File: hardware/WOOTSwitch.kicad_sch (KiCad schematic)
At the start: 67 parts, among them J1 Mini-DIN-4-G, J10 POWSEL, J11 TWI, J12 TWI, J2 Mini-DIN-4-G, J7 Barrel_Jack_MountingPin, J8 EXT_POW, J9 SW1, Q1 MMBT3904, Q11 2N7002, Q15 2N7002, Q2 MMBT3904, Q3 MMBT3904, Q4 MMBT3904, Q5 MMBT3904, Q6 MMBT3904, Q8 MMBT3904, Q9 2N7002, SW1 Switch1, U1 Pico, U2 LM1117-5.0

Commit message: Rebrand as WOOTSwitch
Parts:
- removed C1: 100uF, Capacitor_THT:CP_Radial_D6.3mm_P2.50mm, symbol Device:C_Polarized_US
- removed SW1: Switch1, Button_Switch_THT:SW_SPST_Omron_B3F-315x_Angled, symbol Switch:SW_Push
- added C1, C15: 47uF, Capacitor_SMD:C_1206_3216Metric, symbol Device:C
- added SW2: 1825910-6, hootswitch:SW_1825910-6-4, symbol hootswitch:1825910-6
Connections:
- net GND: now also C1.2, C15.2, SW2.4
- net SWITCH: now also SW2.2
- net at D7.2 (A), J10.1 (Pin_1), U2.2 (VO): now also C1.1, C15.1
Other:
- sheet hootswitch-computers renamed WOOTSwitch-computers
- sheet WOOTSwitch-computers: file hootswitch-computers.kicad_sch -> WOOTSwitch-computers.kicad_sch
- company: (none) -> Joe's Computer Museum
- title: hootswitch -> WOOTSwitch
- moved on the sheet: D7, J10

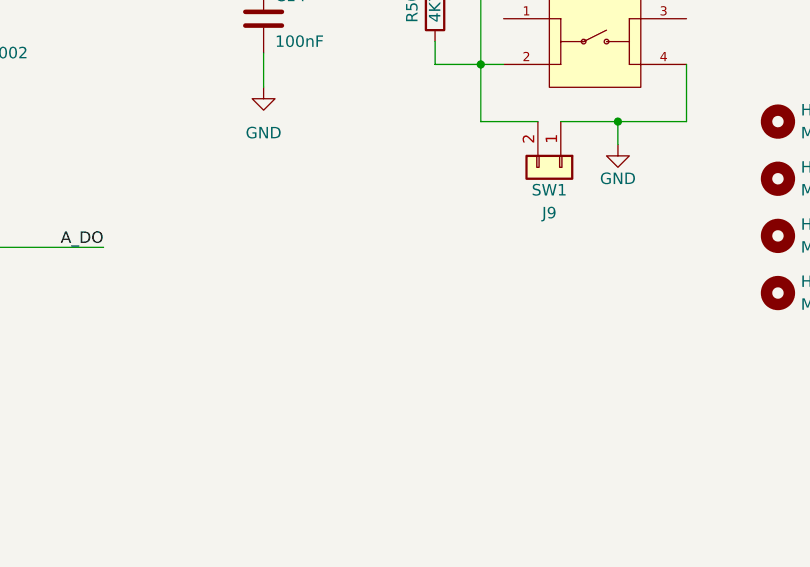
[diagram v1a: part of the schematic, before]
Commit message: Add sheet for power net
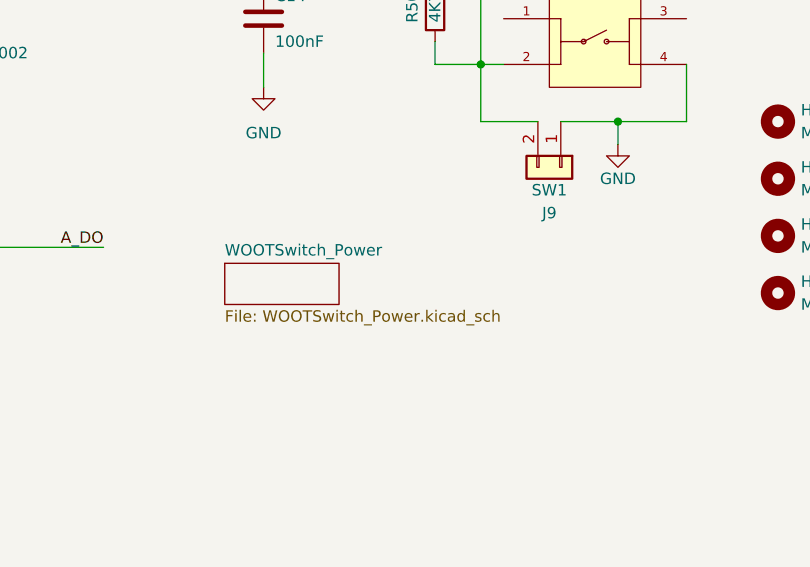
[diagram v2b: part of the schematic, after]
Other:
- added sheet WOOTSwitch_Power (WOOTSwitch_Power.kicad_sch)
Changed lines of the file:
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@@
+		)
+	)
+	(sheet
+		(at 129.032 225.298)
+		(size 12.7 4.572)
+		(exclude_from_sim no)
+		(in_bom yes)
+		(on_board yes)
+		(dnp no)
+		(fields_autoplaced yes)
+		(stroke
+			(width 0.1524)
+			(type solid)
+		)
+		(fill
+			(color 0 0 0 0.0000)
+		)
+		(property "Sheetname" "WOOTSwitch_Power"
+			(at 129.032 224.5864 0)
+			(effects
+				(font
+					(size 1.27 1.27)
+				)
+				(justify left bottom)
+			)
+		)
+		(property "Sheetfile" "WOOTSwitch_Power.kicad_sch"
+			(at 129.032 230.4546 0)
+			(effects
+				(font
+					(size 1.27 1.27)
+				)
+				(justify left top)
+			)
+		)
+		(instances
+			(project "WOOTSwitch"
+				(path "/b47c0368-c762-4e4f-89b1-8c49875ea556"
+					(page "3")
+				)
+			)
 		)
 	)

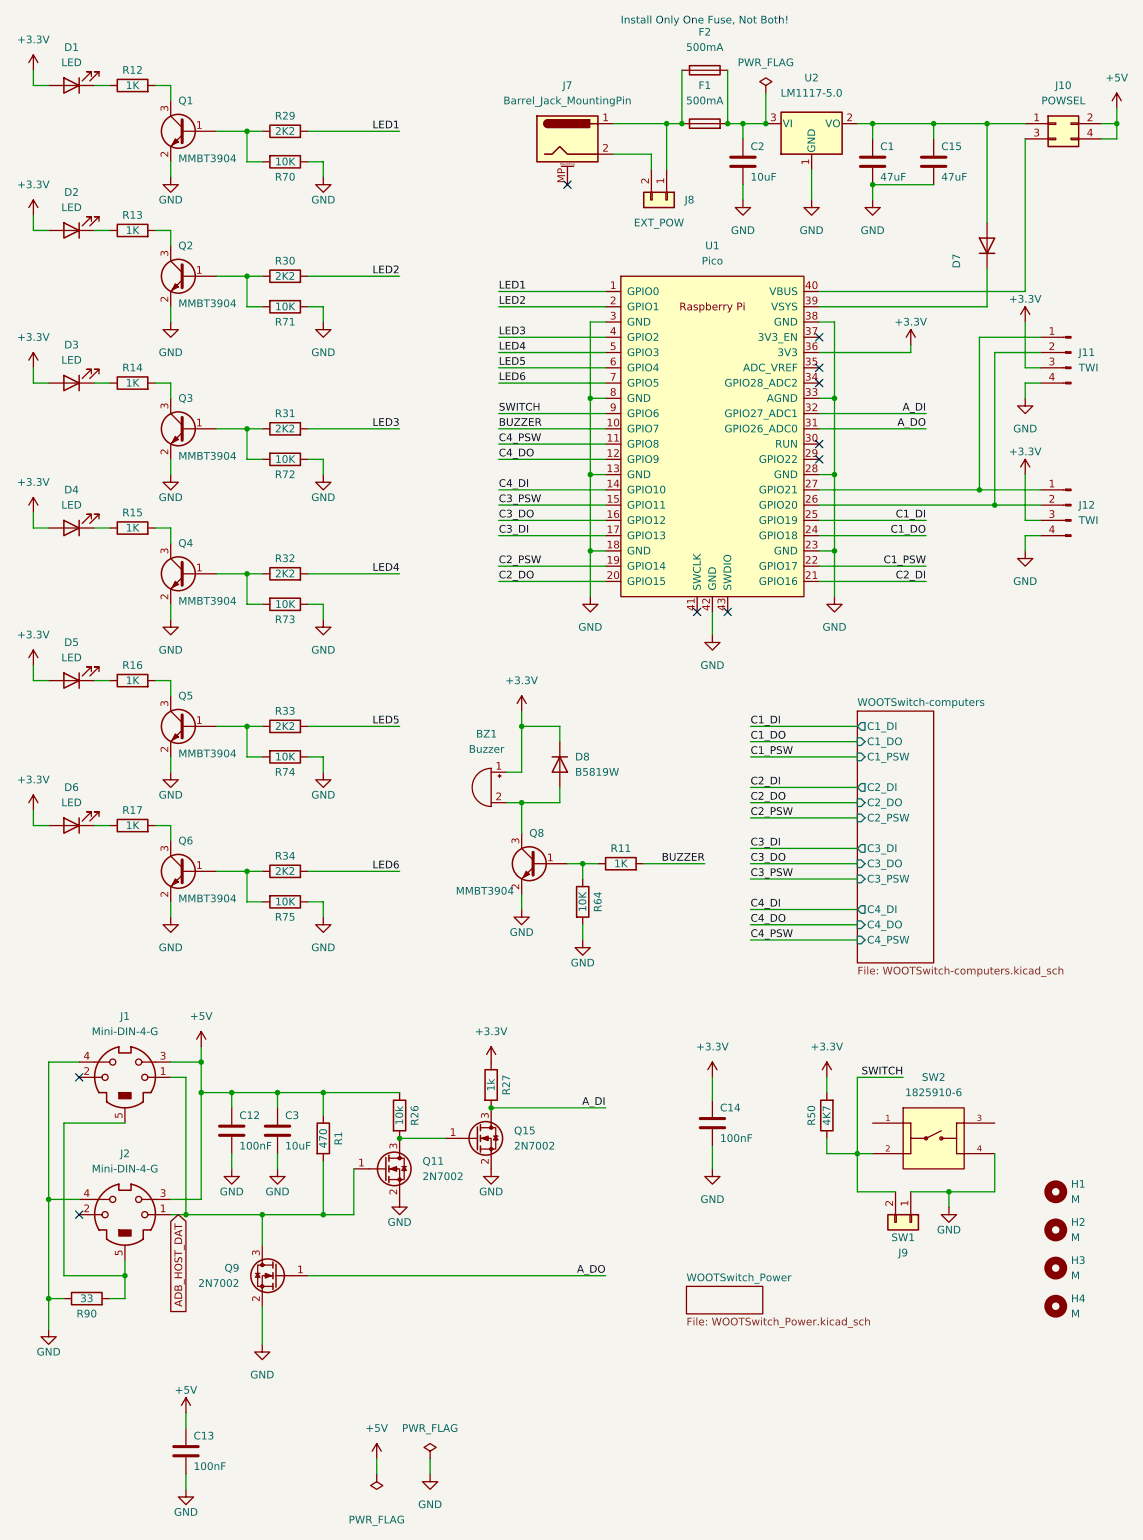
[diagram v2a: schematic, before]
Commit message: Moved mounting holes
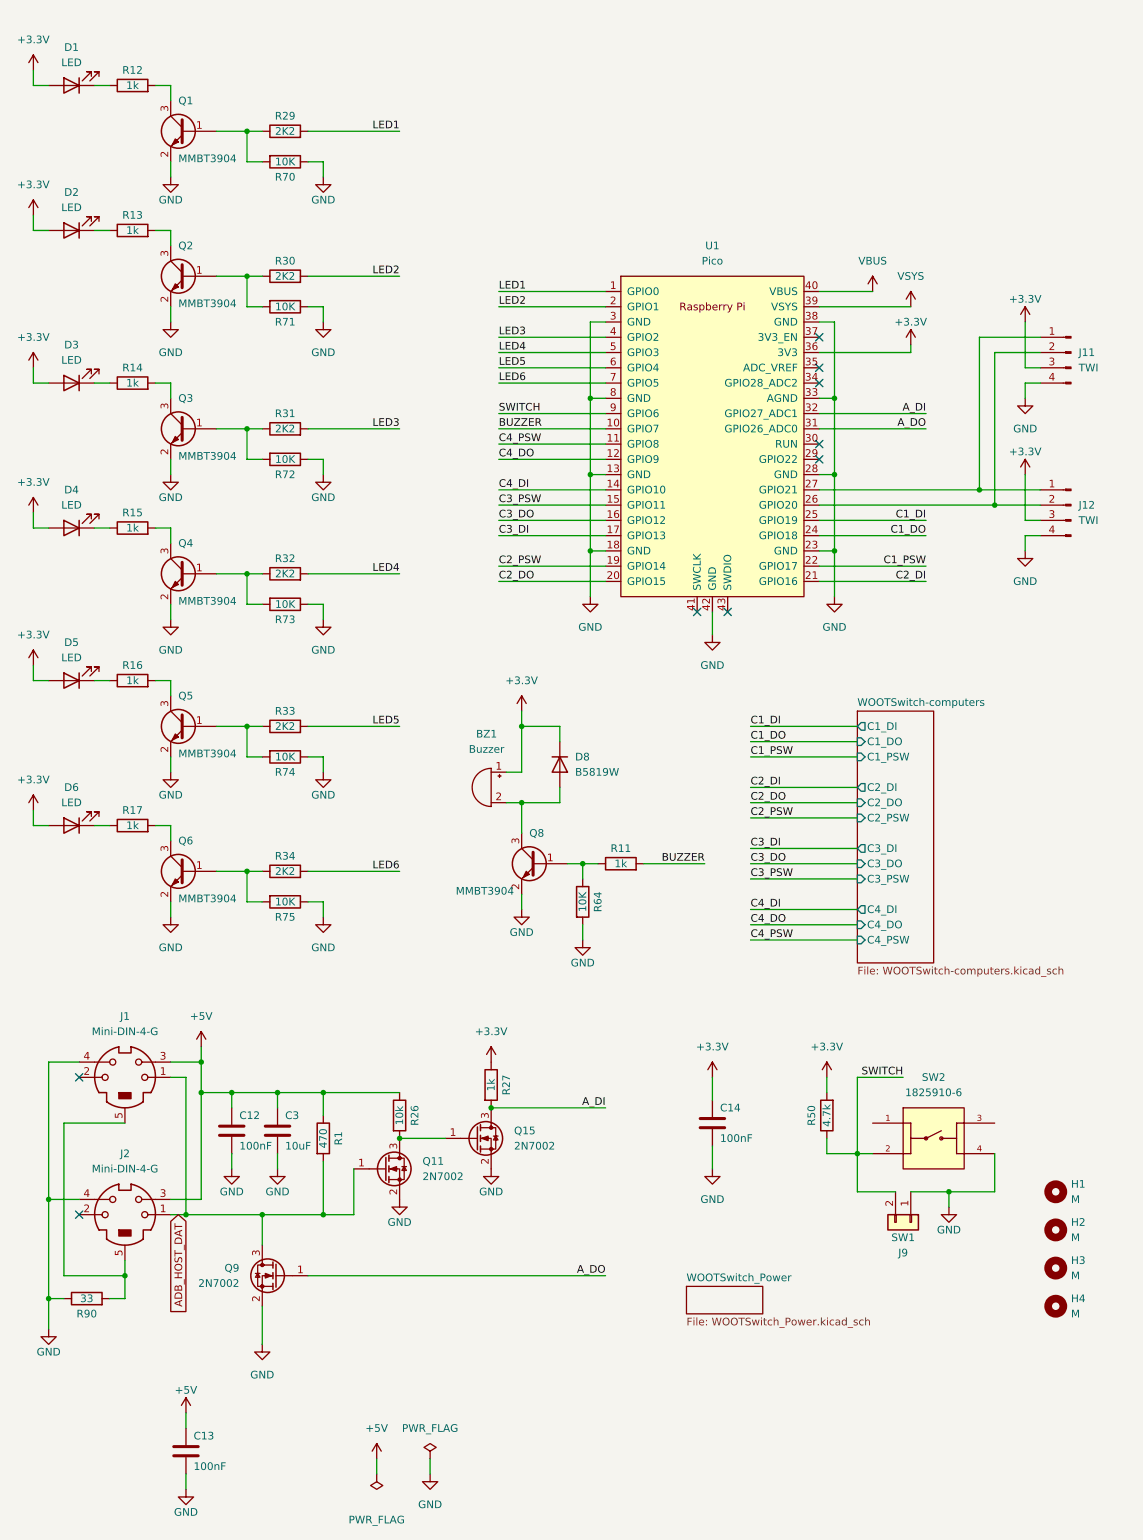
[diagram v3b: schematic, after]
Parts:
- removed C1, C15: 47uF, Capacitor_SMD:C_1206_3216Metric, symbol Device:C
- removed C2: 10uF, Capacitor_SMD:C_0805_2012Metric, symbol Device:C
- removed D7: ${SIM.PARAMS}, Diode_SMD:D_SOD-123, symbol Device:D
- removed F1: 500mA, Fuse:Fuse_Littelfuse_372_D8.50mm, symbol Device:Fuse
- removed F2: 500mA, Fuse:Fuse_0805_2012Metric, symbol Device:Fuse
- removed J10: POWSEL, Connector_PinHeader_2.54mm:PinHeader_2x02_P2.54mm_Vertical, symbol Connector_Generic:Conn_02x02_Odd_Even
- removed J7: Barrel_Jack_MountingPin, Connector_BarrelJack:BarrelJack_CUI_PJ-063AH_Horizontal_CircularHoles, symbol Connector:Barrel_Jack_MountingPin
- removed J8: EXT_POW, Connector_PinHeader_2.54mm:PinHeader_1x02_P2.54mm_Vertical, symbol Connector_Generic:Conn_01x02
- removed U2: LM1117-5.0, Package_TO_SOT_SMD:SOT-223-3_TabPin2, symbol Regulator_Linear:LM1117-5.0
- R11, R12, R13, R14, R15, R16, R17: value 1K -> 1k
- R50: value 4K7 -> 4.7k
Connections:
- net VSYS: now reaches U1.39 (VSYS)
- net VBUS: now reaches U1.40 (VBUS)
- no-connect marks 10 -> 9
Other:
- note removed: "Install Only One Fuse, Not Both!"
